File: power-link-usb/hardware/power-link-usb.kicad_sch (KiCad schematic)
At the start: 30 parts, among them J1 KitProg3, J102 DX07S016JA3, J103 NE8FAH, J104 NE8FAH, Q101 BSC010N04LS, Q102 BSC010N04LS, U101 CYPM1311-48LDXI

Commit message: Update power-link-usb
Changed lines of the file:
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@@
 	(title_block
 		(title "V2 Power Link USB")
-		(date "2026-01-25")
-		(rev "1")
+		(date "2026-02-10")
+		(rev "2026-02-10")
 		(company "Versio Duo")
 	)
@@
 		(at 210.82 177.8 0)
 		(unit 1)
-		(exclude_from_sim no)
+		(exclude_from_sim yes)
 		(in_bom no)
 		(on_board yes)
@@
 			)
 		)
-		(property "Sim.Enable" "0"
-			(at 210.82 177.8 0)
-			(effects
-				(font
-					(size 1.27 1.27)
-				)
-				(hide yes)
-			)
-		)
 		(instances
 			(project ""
@@
 			)
 		)
-		(property "Description" "Nonsensical pad order, the cable's wire 1 is pin 2"
+		(property "Description" "Nonsensical pin order, the cable's wire 1 is pin 2"
 			(at 248.92 58.42 0)
 			(effects
@@
 			(name "V2_A4.kicad_wks")
 			(type worksheet)
-			(data |KLUv/WBZBh0QAGbYTSEQtRsmZc5q276ayLS71D6kxbkmoTeIJM7lAHtEAMAAxQFFAD4ARAB5A7XX
-				+Feo6DSb854N+bVfoZpo+8iKL/InAACB8PMuzmkhNWk9175Qdsa/Zb++KSgopVSdtS+2YnYQARAQ
-				PSHN2zrrIQSbh56z34y7/3r2lJ4Of1z79/bbOd/e/eC8tey/DoK4q13bu46gXRX9eXtRynZwu995
-				BvE/5kL8nI3Nk/a1m00dpgRVsrLGQ7MuGHaRBs3w3x455zH7X+961NgXP52qNm2MterJcdykFCDw
-				F2toV7VFHEoq+0X+3FeTqmrPahTl7toPgcKhzs5+29sEzSaWRPZ4txDEjpmZNCoSioM0SEgak8yy
-				IJj3Ya4p2lMRya6MNJCe7XfnYFNgKAm8i6ITyoVdGMsCckudc06HV6DhQIQUUkMjWpgkwwFgRKZG
-				6xhi9rIXa5JR2G7VLaUWIyB3Y/esXA61A60cum1kagkjQBdbLFpK7bLTBUoaFoLeDQzVgRLQP8C7
-				IFgGOinFH4GJsIkkmr8A6mGAU+bM/Am8LCEJifgkOyfSKPhw4th7Qnfu2ssKvhkRwKHkEg1EDki1
-				zawEeEiIeQ9DuyHXCoZrb2RW4ja+gMkr8fEoLss8oo/dcdIqtN9gDfzh9Q7uaO0X9BOwREYTxRXv
-				f9ciZjvkDpB6gKkC|
+			(data |KLUv/WBhBk0QALbYTiEQtRsmZc5q276ayLS71D6kxbkmoTeIJM7lAHtEAMAAxQFGAD8ARQCbvIHa
+				a/wrVHSazXnPhvzar1BNtH1kxRf5EwCAQPh5F+e0kJq0nmtfKDvj37Jf3xQUlFKqztoXWzE7iAAI
+				iJ6Q5m2d9RAC9jcPPWe/GXf/9ewpPR3+uPbv7bdzvr37wXlr2X8dBHFXu7Z3HUG7Kvrz9qKU7eB2
+				v/MM4n/Mhfg5G5sn7WsDTS2mA1WyssZDsy4YdpEGzfD8Ny+85JzH7H+961FjX/x0qtq0MdaqJ8dx
+				k1KAwF+soV3VFnEoqewX+XNfTaqqPatRlLsbgcKhzs5+29sEzSaWRPZ4txDEjpmZNCoSiiMhaUwy
+				y4Jg3oe5pmhPRSS7MtJAerbfnYNNgaEkuCg6oVzYhbEsF1vRgtxS55zTIVig4URjFFJTI1qYFNIB
+				YESmRusYYvaiF0uSUdhu1Q2lFiOgdmN7VvaH2oWyw9MQXRuZtQQQoIsxFn2ldtnpQiUNa0HvDQCK
+				f/XTisCgEJQEXe/if4EJsakkqj8BMmGAU+ZM/AG8LSEJMfgkOKfSKPhw4rD3ZHfmNZYNfDMigEPJ
+				EBoIDghtm1kJ8BAQ8xyGdkOuFQy33sishFt8DZNX4uNRXJZ5hBy746RJaNtgbfyB613d0dov6Cdg
+				iUQT9BXkf9EiYDuODpB6gKkC|
 			)
-			(checksum "6817F89AF9F875B8ABB3EEDEC3A35A01")
+			(checksum "0A61268C685EAF945CA2EA8187370BD3")
 		)
 	)

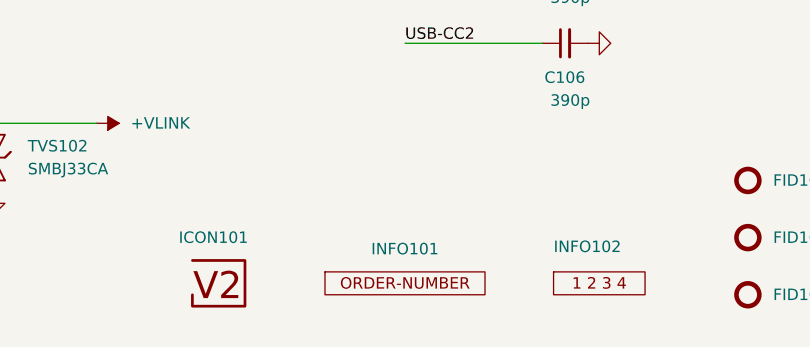
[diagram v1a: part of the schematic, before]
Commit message: Replace Order_Number
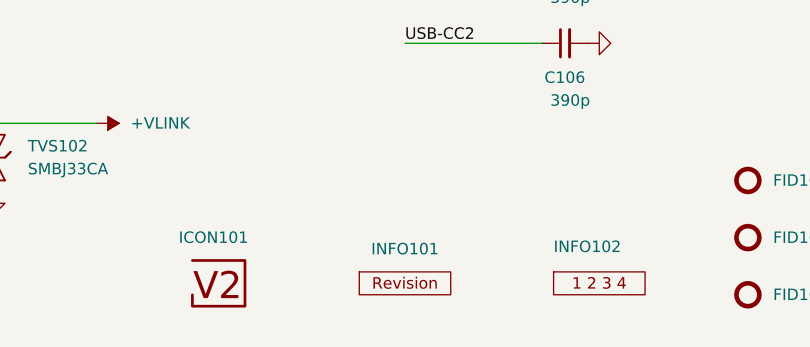
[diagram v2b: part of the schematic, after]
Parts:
- INFO101: value Order_Number -> (none); footprint V2_Production:Order_Number -> V2_Production:Revision; symbol V2_Production:Order_Number -> V2_Production:Revision
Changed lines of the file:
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@@
 		(at 210.82 177.8 0)
 		(unit 1)
-		(exclude_from_sim yes)
+		(exclude_from_sim no)
 		(in_bom no)
 		(on_board yes)
@@
 	)
 	(symbol
-		(lib_id "V2_Production:Order_Number")
+		(lib_id "V2_Production:Revision")
 		(at 231.14 177.8 0)
 		(unit 1)
@@
 			)
 		)
-		(property "Value" "Order_Number"
+		(property "Value" ""
 			(at 231.14 180.34 0)
 			(effects
@@
 			)
 		)
-		(property "Footprint" "V2_Production:Order_Number"
+		(property "Footprint" "V2_Production:Revision"
 			(at 231.14 182.88 0)
 			(effects

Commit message: Update Library
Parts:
- C101: symbol V2_Device:C_0603_10u -> V2_Capacitor:0603_10u
- C102, C103, C104: symbol V2_Device:C_0603_0u1 -> V2_Capacitor:0603_0u1
- C105, C106: symbol V2_Device:C_0603_390p -> V2_Capacitor:0603_390p
- C107: symbol V2_Device:C_0805_10u -> V2_Capacitor:0805_10u
- C108: symbol V2_Device:C_0603_1u -> V2_Capacitor:0603_1u
- D101: symbol V2_Device:LED_0603_Orange -> V2_LED:0603_Orange
- D102: symbol V2_Device:LED_0603_Red -> V2_LED:0603_Red
- R101: symbol V2_Device:R_0603_10k -> V2_Resistor:0603_10k
- R102, R103: symbol V2_Device:R_0603_3k9 -> V2_Resistor:0603_3k9
- R104, R105: symbol V2_Device:R_0603_330R -> V2_Resistor:0603_330R

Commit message: Refresh
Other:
- note added: "PoE Passive +28V IEEE 802.3af Mode B"
- note removed: "PoE Passive +24V IEEE 802.3af Mode B"
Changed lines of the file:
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@@
 		(company "Versio Duo")
 	)
-	(text "PoE Passive +24V\nIEEE 802.3af Mode B"
+	(text "PoE Passive +28V\nIEEE 802.3af Mode B"
 		(exclude_from_sim no)
 		(at 50.038 155.448 0)

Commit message: Export stencil
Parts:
- INFO101: value (none) -> ~
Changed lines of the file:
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@@
 	(title_block
 		(title "V2 Power Link USB")
-		(date "2026-02-10")
+		(date "2026-02-25")
 		(rev "2026-02-10")
 		(company "Versio Duo")
@@
 			)
 		)
-		(property "Value" ""
+		(property "Value" "~"
 			(at 231.14 180.34 0)
 			(effects
